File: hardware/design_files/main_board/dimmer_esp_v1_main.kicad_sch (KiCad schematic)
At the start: 52 parts, among them IC1 PEC11S-929K-S0015, J1 Screw_Terminal_01x03, J2 SM05B-SRSS-TB_LF__SN_, J3 Conn_01x02, K1 FTR-LYCA005Y, Q1 BC817, SW1 Commission, SW2 Toggle, SW3 Reset, U1 SGM2212-3.3XKC3G/TR, U2 USB TYPE-C 16PLT-H10.0, U3 SN74LV1T125DBVR, U4 ESP32-C6-MINI

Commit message: Hardware: Populate C8 (10uF USB VBUS bulk cap)
Remove NC marking from C8. When powered via USB only, the 5V rail
needs local bulk capacitance for stable operation during Zigbee TX
current peaks.

Co-Authored-By: Claude Opus 4.6 (1M context) <noreply@anthropic.com>
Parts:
- C8: value 10uF/25V(20%)(NC) -> 10uF/25V(20%)
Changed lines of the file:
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@@
 			)
 		)
-		(property "Value" "10uF/25V(20%)(NC)"
+		(property "Value" "10uF/25V(20%)"
 			(at 171.45 29.21 90)
 			(effects

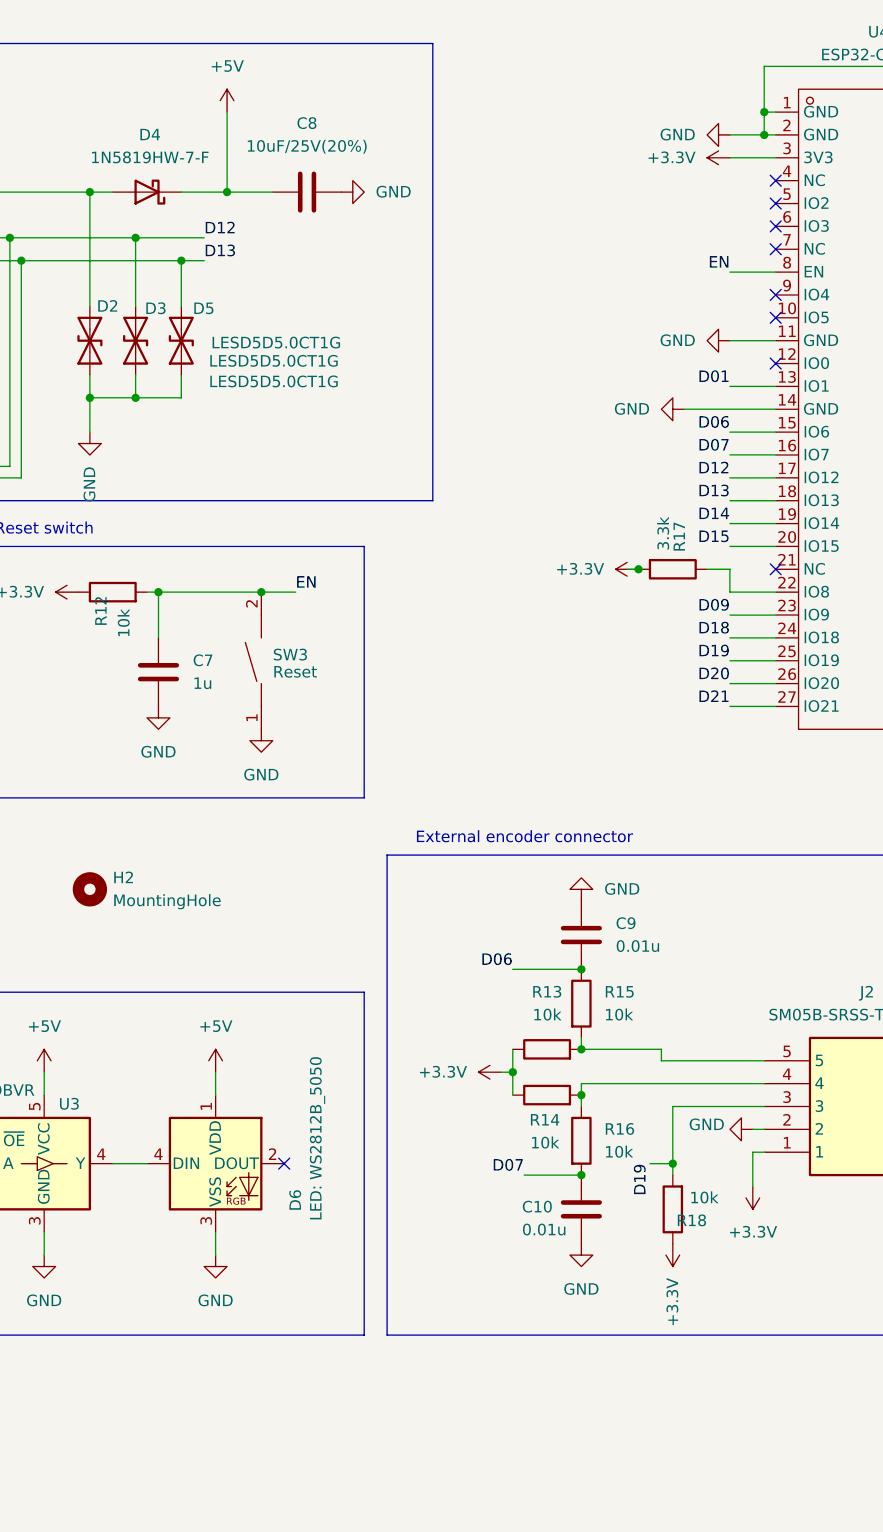
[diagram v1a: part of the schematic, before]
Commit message: Hardware: Add bypass capacitors for ESP32 and WS2812B
Add C11 (0.1uF) near the ESP32-C6 3V3 pin for local decoupling.
Espressif recommends bypass caps close to the module to handle
current peaks during Zigbee TX bursts.

Add C12 (0.1uF) between WS2812B VDD and VSS as recommended by
the WS2812B datasheet to prevent data corruption and flickering.

Co-Authored-By: Claude Opus 4.6 (1M context) <noreply@anthropic.com>
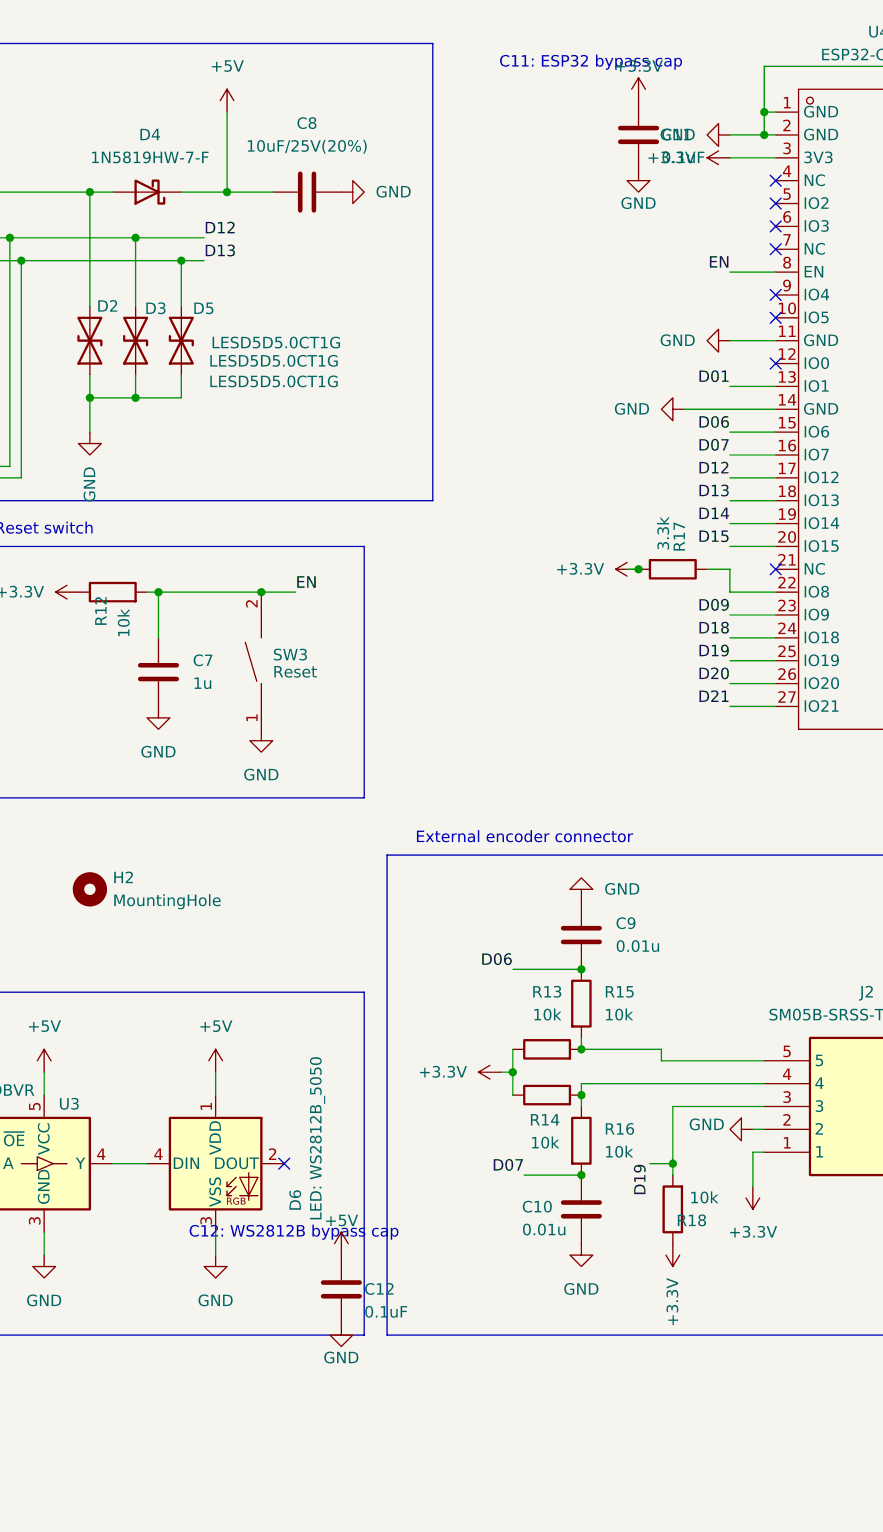
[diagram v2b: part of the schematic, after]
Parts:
- added C11, C12: 0.1uF, Capacitor_SMD:C_0603_1608Metric, symbol Device:C
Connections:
- net +3.3V: now also C11.1
- net +5V: now also C12.1
- net GND: now also C11.2, C12.2
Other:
- note added: "C11: ESP32 bypass cap"
- note added: "C12: WS2812B bypass cap"
